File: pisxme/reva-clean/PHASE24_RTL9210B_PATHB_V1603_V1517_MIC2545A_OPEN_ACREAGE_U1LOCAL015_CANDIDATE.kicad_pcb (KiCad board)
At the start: 6 copper layers, 100.1 x 55.1 mm, 17 parts, among them J1 M.2 Socket 3 M-key 2280, U1 RTL9210B-CG, U2 W25Q128_SPI_FLASH, U3 MIC2545A-1YM, Y1 XTAL_25MHz

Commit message: phase24: apply local QFN rule to support candidate
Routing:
- net GND: track 51.4 -> 49.8 mm, vias 9 -> 7
- net SSD_3V3: vias 2 -> 3

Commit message: phase24: close support candidate ground and via defects
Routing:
- net GND: track 49.8 -> 83.8 mm, vias 7 -> 9
- net SSD_3V3: vias 3 -> 2
- net RTL_3V3: vias 12 -> 11
- net ISOLATEB: vias 3 -> 2

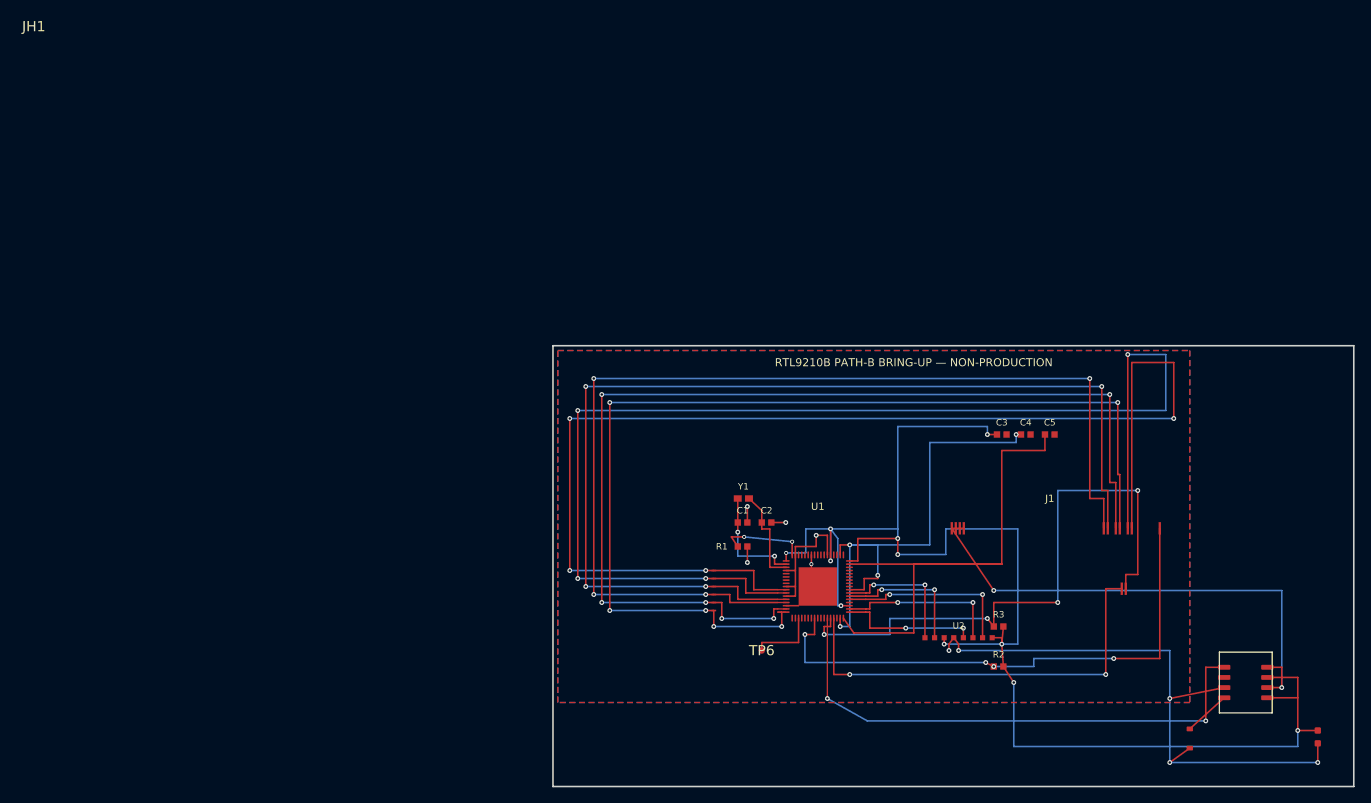
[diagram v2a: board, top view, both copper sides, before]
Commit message: phase24: close local RTL9210B QFN handoff
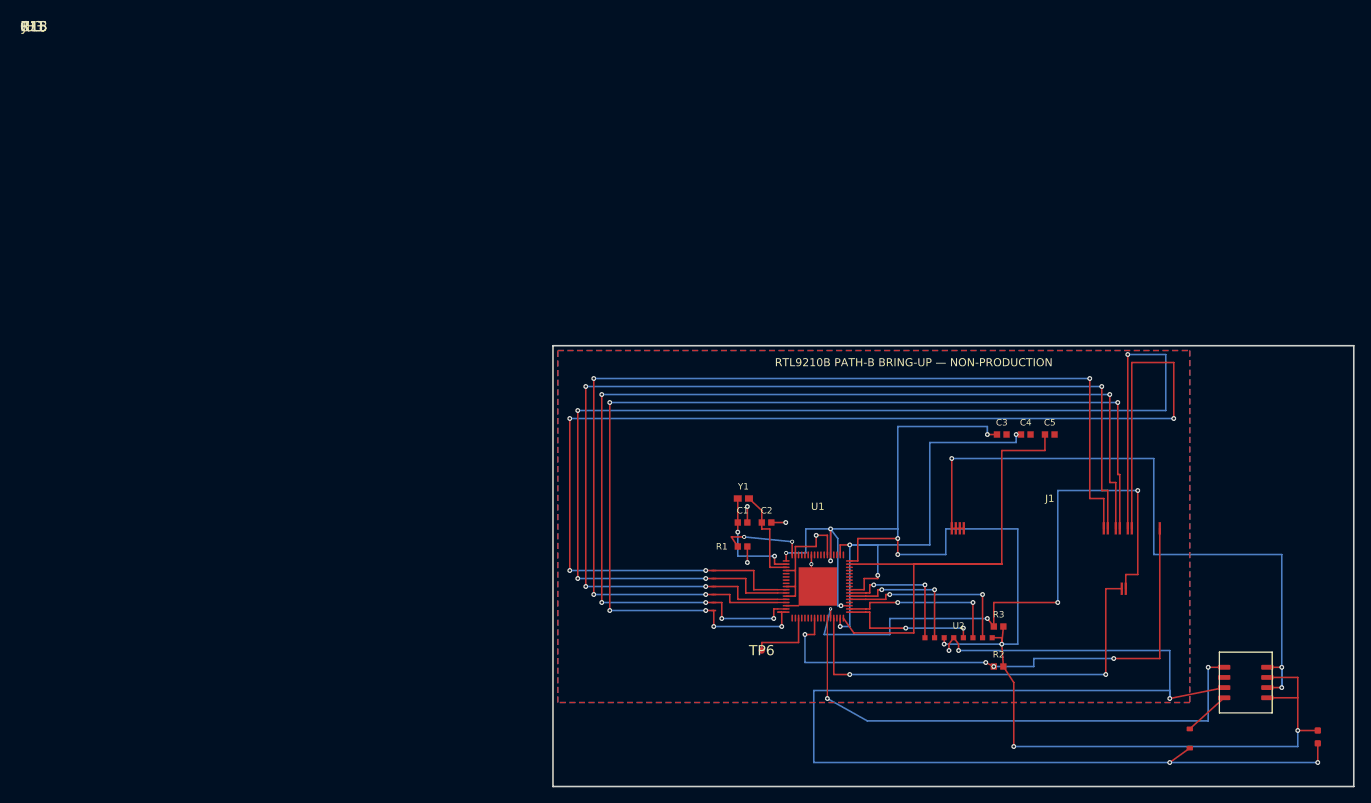
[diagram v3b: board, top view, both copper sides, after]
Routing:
- net GND: track 83.8 -> 174.8 mm
- net SSD_3V3: track 65.2 -> 86.3 mm, vias 2 -> 3
- net CLKREQ_N: track 75.3 -> 76.9 mm
